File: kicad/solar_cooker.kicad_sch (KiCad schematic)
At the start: 28 parts, among them J1 Pt100, J10 SSQ-108-01-G-S, J11 SSQ-108-01-G-S, J12 SSQ-108-01-G-S, J13 SSQ-118-01-G-D, J14 SSQ-108-01-G-S, J15 SSQ-108-01-G-S, J16 SSQ-110-01-G-S, J4 Pt100, J6 GPS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

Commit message: project files rename + connector improvement
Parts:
- removed J10, J11, J12, J14, J15: SSQ-108-01-G-S, SSQ-108-01-G-S:SAMTEC_SSQ-108-01-G-S, symbol SSQ-108-01-G-S:SSQ-108-01-G-S
- removed J13: SSQ-118-01-G-D, SAMTEC_SSQ-118-01-G-D, symbol SSQ-118-01-G-D:SSQ-118-01-G-D
- removed J16: SSQ-110-01-G-S, SAMTEC_SSQ-110-01-G-S, symbol SSQ-110-01-G-S:SSQ-110-01-G-S
- removed J9: SSQ-109-01-G-S, SAMTEC_SSQ-109-01-G-S, symbol SSQ-109-01-G-S:SSQ-109-01-G-S
- A1: AVAILABILITY Unavailable -> (none); DESCRIPTION Dev.kit: Arduino; SPI, TWI, UART; ICSP, USB B, pin strips, 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 -> (none); MF Arduino -> (none); MP ARDUINO MEGA2560 REV3 - RETAIL -> (none); PACKAGE None -> (none); PRICE None -> (none)
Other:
- added sheet connectors (connectors.kicad_sch)

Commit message: Electrical Rules Checker fix
there are still some issues that need to be resolved
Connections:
- net D43: no longer names the net of A1.43
- net D45: no longer names the net of A1.45
- no-connect marks 85 -> 87
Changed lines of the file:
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@@
   (no_connect (at 215.265 70.485))
   (no_connect (at 102.235 113.03))
+  (no_connect (at 215.265 131.445))
   (no_connect (at 102.235 100.33))
   (no_connect (at 255.905 111.125))
@@
   (no_connect (at 255.905 34.925))
   (no_connect (at 215.265 52.705))
+  (no_connect (at 215.265 133.985))
   (no_connect (at 215.265 111.125))
   (no_connect (at 255.905 32.385))
@@
     (stroke (width 0) (type default))
   )
-  (wire (pts (xy 208.915 133.985) (xy 215.265 133.985))
-    (stroke (width 0) (type default))
-  )
   (wire (pts (xy 122.555 118.11) (xy 126.365 118.11))
     (stroke (width 0) (type default))
@@
     (stroke (width 0) (type default))
   )
-  (wire (pts (xy 208.915 131.445) (xy 215.265 131.445))
-    (stroke (width 0) (type default))
-  )
   (wire (pts (xy 126.365 113.03) (xy 122.555 113.03))
     (stroke (width 0) (type default))
@@
     (effects (font (size 1.27 1.27)) (justify right bottom))
   )
-  (label "D45" (at 208.915 133.985 0) (fields_autoplaced)
-    (effects (font (size 1.27 1.27)) (justify left bottom))
-  )
   (label "MISO" (at 62.484 159.385 180) (fields_autoplaced)
     (effects (font (size 1.27 1.27)) (justify right bottom))
@@
     (effects (font (size 1.27 1.27)) (justify right bottom))
   )
-  (label "D43" (at 208.915 131.445 0) (fields_autoplaced)
-    (effects (font (size 1.27 1.27)) (justify left bottom))
-  )
   (label "MISO" (at 130.175 105.41 180) (fields_autoplaced)
     (effects (font (size 1.27 1.27)) (justify right bottom))
@@
     )
     (property "SPN" "SAM1180-09-ND" (at 112.395 107.95 0)
+      (effects (font (size 1.27 1.27)) hide)
+    )
+    (property "Sim.Enable" "0" (at 112.395 107.95 0)
       (effects (font (size 1.27 1.27)) hide)
     )
@@
       (effects (font (size 1.27 1.27)) hide)
     )
+    (property "Sim.Enable" "0" (at 52.07 120.015 0)
+      (effects (font (size 1.27 1.27)) hide)
+    )
     (pin "1")
     (pin "2")
@@
       (effects (font (size 1.27 1.27)) hide)
     )
+    (property "Sim.Enable" "0" (at 153.035 35.56 0)
+      (effects (font (size 1.27 1.27)) hide)
+    )
     (pin "1")
     (pin "2")
@@
     )
     (property "SPN" "SAM1180-08-ND" (at 52.07 35.56 0)
+      (effects (font (size 1.27 1.27)) hide)
+    )
+    (property "Sim.Enable" "0" (at 52.07 35.56 0)
       (effects (font (size 1.27 1.27)) hide)
     )
@@
       (effects (font (size 1.27 1.27)) hide)
     )
+    (property "Sim.Enable" "0" (at 75.946 160.528 0)
+      (effects (font (size 1.27 1.27)) hide)
+    )
     (pin "1")
     (pin "2")
@@
       (effects (font (size 1.27 1.27)) hide)
     )
+    (property "Sim.Enable" "0" (at 137.16 35.56 0)
+      (effects (font (size 1.27 1.27)) hide)
+    )
     (pin "1")
     (pin "2")
@@
       (effects (font (size 1.27 1.27)) hide)
     )
+    (property "Sim.Enable" "0" (at 85.09 64.135 0)
+      (effects (font (size 1.27 1.27)) hide)
+    )
     (pin "1")
     (pin "2")
@@
     )
     (property "SPN" "SAM1180-08-ND" (at 42.037 160.655 0)
+      (effects (font (size 1.27 1.27)) hide)
+    )
+    (property "Sim.Enable" "0" (at 42.037 160.655 0)
       (effects (font (size 1.27 1.27)) hide)
     )
@@
       (effects (font (size 1.27 1.27)) hide)
     )
+    (property "Sim.Enable" "0" (at 108.966 160.528 0)
+      (effects (font (size 1.27 1.27)) hide)
+    )
     (pin "1")
     (pin "2")
@@
       (effects (font (size 1.27 1.27)) hide)
     )
+    (property "Sim.Enable" "0" (at 52.07 94.615 0)
+      (effects (font (size 1.27 1.27)) hide)
+    )
     (pin "1")
     (pin "2")
@@
     )
     (property "Datasheet" "" (at 235.585 88.265 0)
+      (effects (font (size 1.27 1.27)) hide)
+    )
+    (property "Sim.Enable" "0" (at 235.585 88.265 0)
       (effects (font (size 1.27 1.27)) hide)
     )
@@
       (effects (font (size 1.27 1.27)) hide)
     )
+    (property "Sim.Enable" "0" (at 85.09 34.29 0)
+      (effects (font (size 1.27 1.27)) hide)
+    )
     (pin "1")
     (pin "2")
@@
       (effects (font (size 1.27 1.27)) hide)
     )
+    (property "Sim.Enable" "0" (at 113.665 35.56 0)
+      (effects (font (size 1.27 1.27)) hide)
+    )
     (pin "1")
     (pin "2")
@@
     )
     (property "SPN" "SAM1180-09-ND" (at 85.09 102.235 0)
+      (effects (font (size 1.27 1.27)) hide)
+    )
+    (property "Sim.Enable" "0" (at 85.09 102.235 0)
       (effects (font (size 1.27 1.27)) hide)
     )
@@
       (effects (font (size 1.27 1.27)) hide)
     )
+    (property "Sim.Enable" "0" (at 52.07 67.945 0)
+      (effects (font (size 1.27 1.27)) hide)
+    )
     (pin "1")
     (pin "2")
@@
       (effects (font (size 1.27 1.27)) hide)
     )
+    (property "Sim.Enable" "0" (at 124.46 69.215 0)
+      (effects (font (size 1.27 1.27)) hide)
+    )

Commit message: kicad 9V DCDC convertor Vout- fix + rename clock
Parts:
- U3: value clock_module -> clock; footprint custom_components:clock_module -> custom_components:clock; symbol custom_components:clock_module -> custom_components:clock
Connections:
- net GND: now also PS1.3 (-VOUT)
- no-connect marks 87 -> 86
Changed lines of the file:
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@@
   (no_connect (at 102.235 110.49))
   (no_connect (at 255.905 93.345))
-  (no_connect (at 144.78 71.755))
   (no_connect (at 215.265 108.585))
   (no_connect (at 255.905 75.565))
@@
     (stroke (width 0) (type default) (color 0 0 255 1))
   )
+  (wire (pts (xy 144.78 71.755) (xy 146.05 71.755))
+    (stroke (width 0) (type default))
+  )
   (wire (pts (xy 153.035 39.37) (xy 153.035 41.91))
     (stroke (width 0) (type default))
@@
     (stroke (width 0) (type default))
   )
+  (wire (pts (xy 146.05 71.755) (xy 146.05 73.025))
+    (stroke (width 0) (type default))
+  )
   (wire (pts (xy 153.035 46.99) (xy 153.035 49.53))
     (stroke (width 0) (type default))
@@
     (stroke (width 0) (type default) (color 0 0 255 1))
   )
+  (wire (pts (xy 41.275 59.055) (xy 44.45 59.055))
+    (stroke (width 0) (type default) (color 255 0 0 1))
+  )
   (wire (pts (xy 137.16 29.21) (xy 137.16 31.75))
     (stroke (width 0) (type default))
@@
     (stroke (width 0) (type default) (color 0 0 255 1))
   )
-  (wire (pts (xy 35.56 61.595) (xy 44.45 61.595))
+  (wire (pts (xy 38.1 61.595) (xy 44.45 61.595))
     (stroke (width 0) (type default) (color 0 0 0 1))
   )
@@
     (stroke (width 0) (type default) (color 128 77 0 1))
   )
+  (wire (pts (xy 41.275 57.15) (xy 41.275 59.055))
+    (stroke (width 0) (type default) (color 255 0 0 1))
+  )
   (wire (pts (xy 122.555 102.87) (xy 130.175 102.87))
     (stroke (width 0) (type default))
@@
   (wire (pts (xy 39.37 36.83) (xy 44.45 36.83))
     (stroke (width 0) (type default) (color 0 0 255 1))
-  )
-  (wire (pts (xy 35.56 59.055) (xy 44.45 59.055))
-    (stroke (width 0) (type default) (color 255 0 0 1))
   )
   (wire (pts (xy 123.19 38.1) (xy 123.19 40.005))
@@
   )
   (symbol (lib_id "power:+5V") (at 41.275 45.72 180) (unit 1)
-    (in_bom yes) (on_board yes) (dnp no) (fields_autoplaced)
+    (in_bom yes) (on_board yes) (dnp no)
     (property "Reference" "#PWR03" (at 41.275 41.91 0)
       (effects (font (size 1.27 1.27)) hide)
     )
-    (property "Value" "+5V" (at 41.275 49.276 0)
+    (property "Value" "+5V" (at 41.275 49.53 0)
       (effects (font (size 1.27 1.27)))
     )
@@
       (project "solar_cooker"
         (path "/c2c342ae-c172-4b44-a50e-ddd387eb2591"
-          (reference "#PWR07") (unit 1)
+          (reference "#PWR06") (unit 1)
         )
       )
@@
       (project "solar_cooker"
         (path "/c2c342ae-c172-4b44-a50e-ddd387eb2591"
-          (reference "#PWR06") (unit 1)
+          (reference "#PWR05") (unit 1)
         )
       )
@@
     )
   )
-  (symbol (lib_id "power:GND") (at 35.56 61.595 270) (unit 1)
-    (in_bom yes) (on_board yes) (dnp no)
-    (property "Reference" "#PWR06" (at 29.21 61.595 0)
-      (effects (font (size 1.27 1.27)) hide)
-    )
-    (property "Value" "GND" (at 31.75 61.595 0)
-      (effects (font (size 1.27 1.27)))
-    )
-    (property "Footprint" "" (at 35.56 61.595 0)
-      (effects (font (size 1.27 1.27)) hide)
-    )
-    (property "Datasheet" "" (at 35.56 61.595 0)
+  (symbol (lib_id "power:GND") (at 38.1 61.595 270) (unit 1)
+    (in_bom yes) (on_board yes) (dnp no)
+    (property "Reference" "#PWR06" (at 31.75 61.595 0)
+      (effects (font (size 1.27 1.27)) hide)
+    )
+    (property "Value" "GND" (at 34.29 61.595 0)
+      (effects (font (size 1.27 1.27)))
+    )
+    (property "Footprint" "" (at 38.1 61.595 0)
+      (effects (font (size 1.27 1.27)) hide)
+    )
+    (property "Datasheet" "" (at 38.1 61.595 0)
       (effects (font (size 1.27 1.27)) hide)
     )
@@
       (project "solar_cooker"
         (path "/c2c342ae-c172-4b44-a50e-ddd387eb2591"
+          (reference "#PWR04") (unit 1)
+        )
+      )
+    )
+  )
+  (symbol (lib_id "power:+5V") (at 41.275 57.15 0) (unit 1)
+    (in_bom yes) (on_board yes) (dnp no)
+    (property "Reference" "#PWR05" (at 41.275 60.96 0)
+      (effects (font (size 1.27 1.27)) hide)
+    )
+    (property "Value" "+5V" (at 39.37 53.34 0)
+      (effects (font (size 1.27 1.27)) (justify left))
+    )
+    (property "Footprint" "" (at 41.275 57.15 0)
+      (effects (font (size 1.27 1.27)) hide)
+    )
+    (property "Datasheet" "" (at 41.275 57.15 0)
+      (effects (font (size 1.27 1.27)) hide)
+    )
+    (pin "1")
+    (instances
+      (project "solar_cooker"
+        (path "/61392a14-41f9-4325-aa01-94abd722c473"
           (reference "#PWR05") (unit 1)
         )
       )
-    )
-  )
-  (symbol (lib_id "power:+5V") (at 35.56 59.055 90) (unit 1)
-    (in_bom yes) (on_board yes) (dnp no) (fields_autoplaced)
-    (property "Reference" "#PWR05" (at 39.37 59.055 0)
-      (effects (font (size 1.27 1.27)) hide)
-    )
-    (property "Value" "+5V" (at 32.004 59.055 0)
-      (effects (font (size 1.27 1.27)))
-    )
-    (property "Footprint" "" (at 35.56 59.055 0)
-      (effects (font (size 1.27 1.27)) hide)
-    )
-    (property "Datasheet" "" (at 35.56 59.055 0)
-      (effects (font (size 1.27 1.27)) hide)
-    )
-    (pin "1")
-    (instances
-      (project "solar_cooker"
-        (path "/61392a14-41f9-4325-aa01-94abd722c473"
-          (reference "#PWR05") (unit 1)
-        )
-      )
-      (project "solar_cooker"
-        (path "/c2c342ae-c172-4b44-a50e-ddd387eb2591"
-          (reference "#PWR04") (unit 1)
+      (project "solar_cooker"
+        (path "/c2c342ae-c172-4b44-a50e-ddd387eb2591"
+          (reference "#PWR07") (unit 1)
         )
       )
@@
         (path "/c2c342ae-c172-4b44-a50e-ddd387eb2591"
           (reference "J7") (unit 1)
+        )
+      )
+    )
+  )
+  (symbol (lib_id "power:GND") (at 146.05 73.025 0) (unit 1)
+    (in_bom yes) (on_board yes) (dnp no)
+    (property "Reference" "#PWR024" (at 146.05 79.375 0)
+      (effects (font (size 1.27 1.27)) hide)
+    )
+    (property "Value" "GND" (at 146.05 76.835 0)
+      (effects (font (size 1.27 1.27)))
+    )
+    (property "Footprint" "" (at 146.05 73.025 0)
+      (effects (font (size 1.27 1.27)) hide)
+    )
+    (property "Datasheet" "" (at 146.05 73.025 0)
+      (effects (font (size 1.27 1.27)) hide)
+    )
+    (pin "1")
+    (instances
+      (project "solar_cooker_v2"
+        (path "/44c2afa1-48ea-4efe-ab9b-507688a863d4/27b19281-8c9c-419f-90e7-59a0d218fc1a"
+          (reference "#PWR024") (unit 1)
+        )
+      )
+      (project "solar_cooker"
+        (path "/c2c342ae-c172-4b44-a50e-ddd387eb2591"
+          (reference "#PWR038") (unit 1)
         )
       )
@@
     )
   )
-  (symbol (lib_id "custom_components:clock_module") (at 52.07 67.945 0) (unit 1)
+  (symbol (lib_id "custom_components:clock") (at 52.07 67.945 0) (unit 1)
     (in_bom yes) (on_board yes) (dnp no)
     (property "Reference" "U3" (at 52.07 53.975 0)
       (effects (font (size 1.27 1.27)))
     )
-    (property "Value" "clock_module" (at 52.07 56.515 0)
-      (effects (font (size 1.27 1.27)))
-    )
-    (property "Footprint" "custom_components:clock_module" (at 52.07 67.945 0)
-      (effects (font (size 1.27 1.27)) hide)
-    )
+    (property "Value" "clock" (at 52.07 56.515 0)
+      (effects (font (size 1.27 1.27)))
+    )
+    (property "Footprint" "custom_components:clock" (at 52.07 67.945 0)
+      (effects (font (size 1.27 1.27)) hide)
+    )

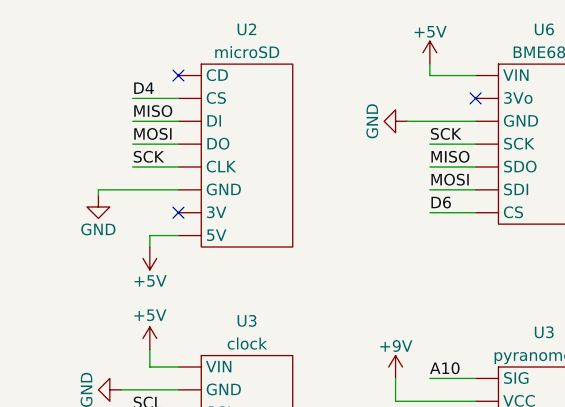
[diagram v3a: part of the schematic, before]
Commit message: microSD module fix kicad
MISO and MOSI flipped
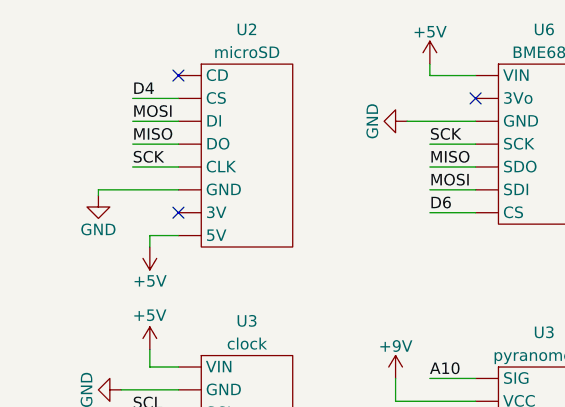
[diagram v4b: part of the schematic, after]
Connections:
- net MISO: now also U2.5 (DO); no longer U2.6 (DI)
- net MOSI: now also U2.6 (DI); no longer U2.5 (DO)
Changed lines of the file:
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@@
-    (effects (font (size 1.27 1.27)) (justify left bottom))
-  )
-  (label "MOSI" (at 39.37 34.29 0) (fields_autoplaced)
     (effects (font (size 1.27 1.27)) (justify left bottom))
   )
@@
     (effects (font (size 1.27 1.27)) (justify right bottom))
   )
+  (label "MOSI" (at 39.37 31.75 0) (fields_autoplaced)
+    (effects (font (size 1.27 1.27)) (justify left bottom))
+  )
   (label "MISO" (at 62.484 159.385 180) (fields_autoplaced)
     (effects (font (size 1.27 1.27)) (justify right bottom))
@@
     (effects (font (size 1.27 1.27)) (justify left bottom))
   )
+  (label "MISO" (at 39.37 34.29 0) (fields_autoplaced)
+    (effects (font (size 1.27 1.27)) (justify left bottom))
+  )
   (label "MOSI" (at 130.175 107.95 180) (fields_autoplaced)
     (effects (font (size 1.27 1.27)) (justify right bottom))
@@
     (effects (font (size 1.27 1.27)) (justify left bottom))
   )
-  (label "MISO" (at 39.37 31.75 0) (fields_autoplaced)
-    (effects (font (size 1.27 1.27)) (justify left bottom))
-  )

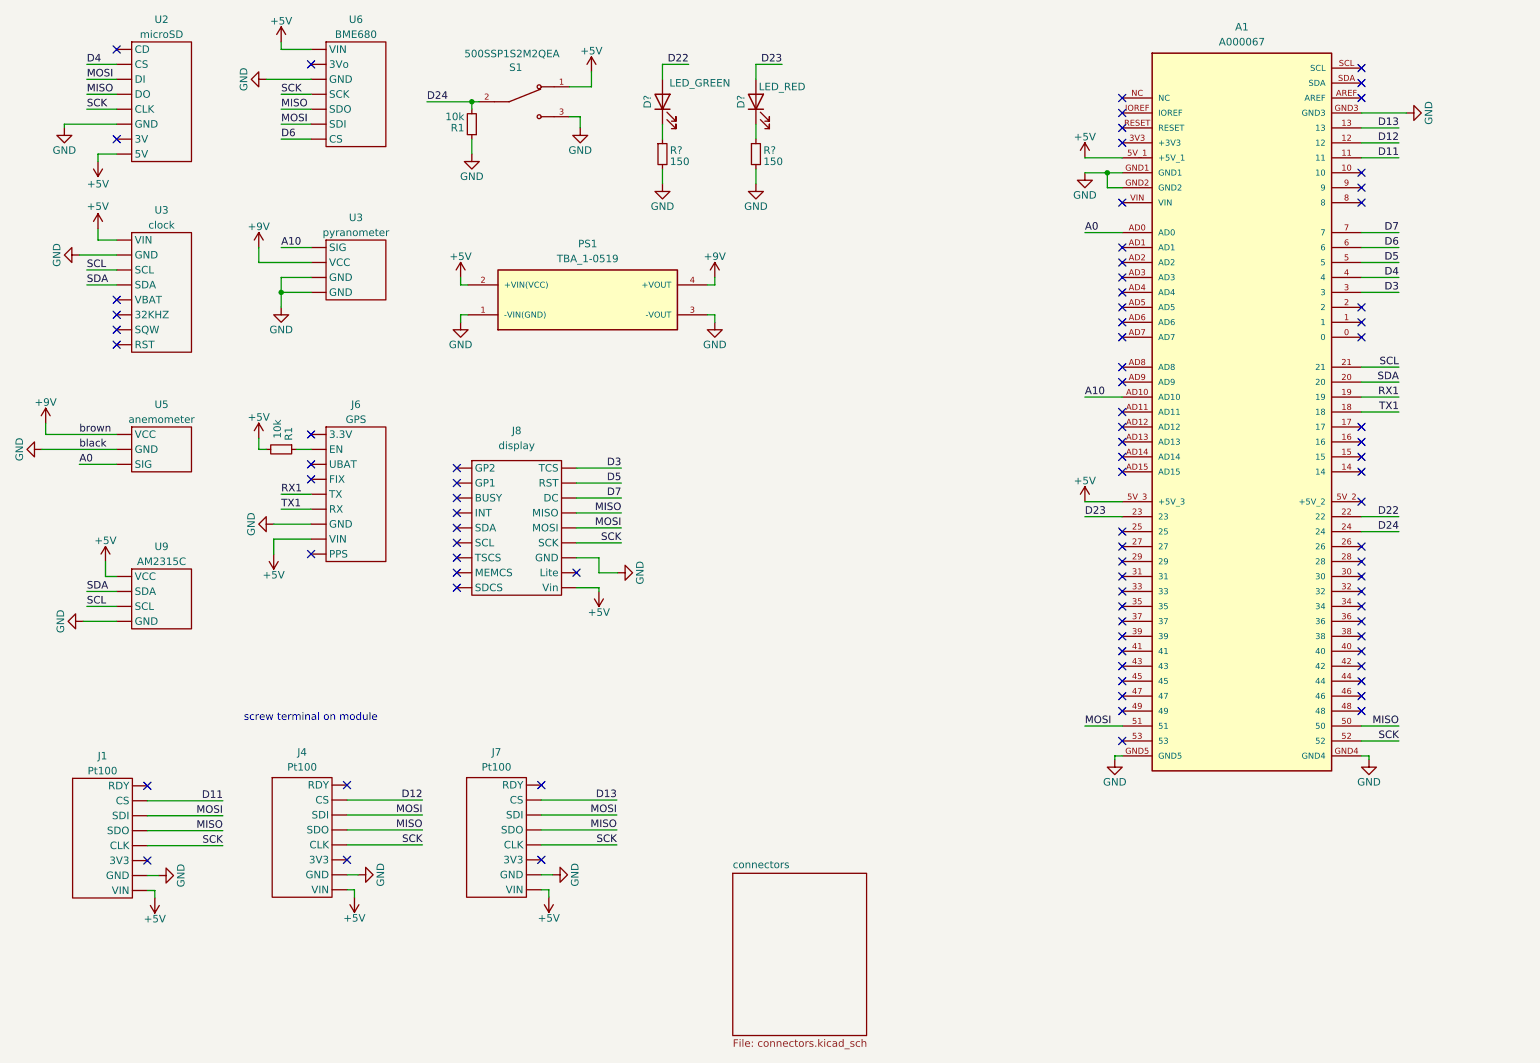
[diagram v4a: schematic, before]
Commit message: silkscreen update + schematic improvements
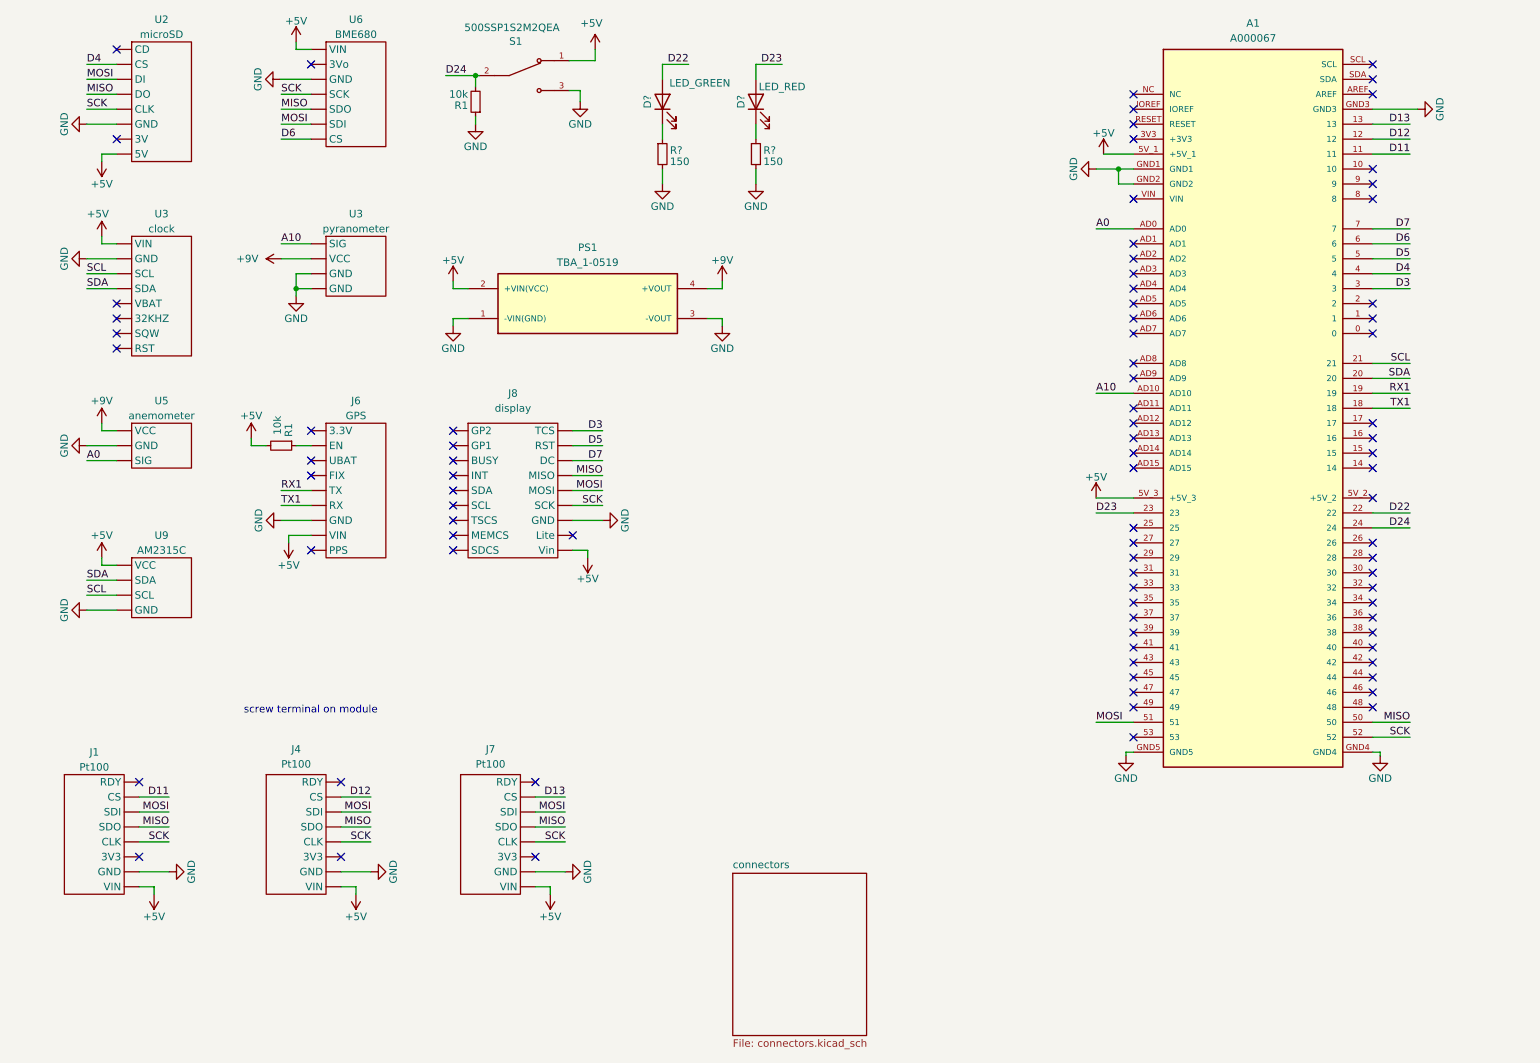
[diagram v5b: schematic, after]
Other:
- moved on the sheet: A1, J1, J4, J6, J7, J8, PS1, R1, S1, U3, U5, U9
